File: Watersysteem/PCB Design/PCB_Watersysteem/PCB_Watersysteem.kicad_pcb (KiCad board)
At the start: 2 copper layers, 98 parts, among them J1 12V ingang, J10 LED Water Level, J11 LED Nutrient Level, J12 Height Nutrients, J13 Height Mixer, J14 Pomp1, J15 Pomp2, J16 Pomp3, J17 Pomp4, J18 Luchtpomp, J19 Mixer, J2 TTL Connector, J20 UV, J22 230V, J23 ReferentieProbe, J24 Voedingsstoffen 1, J25 Voedingsstoffen 2, J26 Voedingsstoffen 3, J6 Height Water, J7 Endstop Lade0, J8 Endstop Lade1, J9 Endstop UV, K1 AHQSS105DM2FA0G, K2 AHQSS105DM2FA0G, K3 AHQSS105DM2FA0G, K6 AHQSS105DM2FA0G, K7 AHQSS105DM2FA0G, K8 AHQSS105DM2FA0G, K9 AHQSS105DM2FA0G, Q1 BSS138, Q2 BSS138, Q3 BSS138, Q4 BSS138, Q5 BSS138, Q6 BSS138, Q7 BSS138, SW1 EN, SW2 BOOT, U1 ESP32-WROOM-32D, U2 MP1584_Module, U3 AMS1117-3.3, U4 ADS1115IDGS, U5 MCP23017_SO

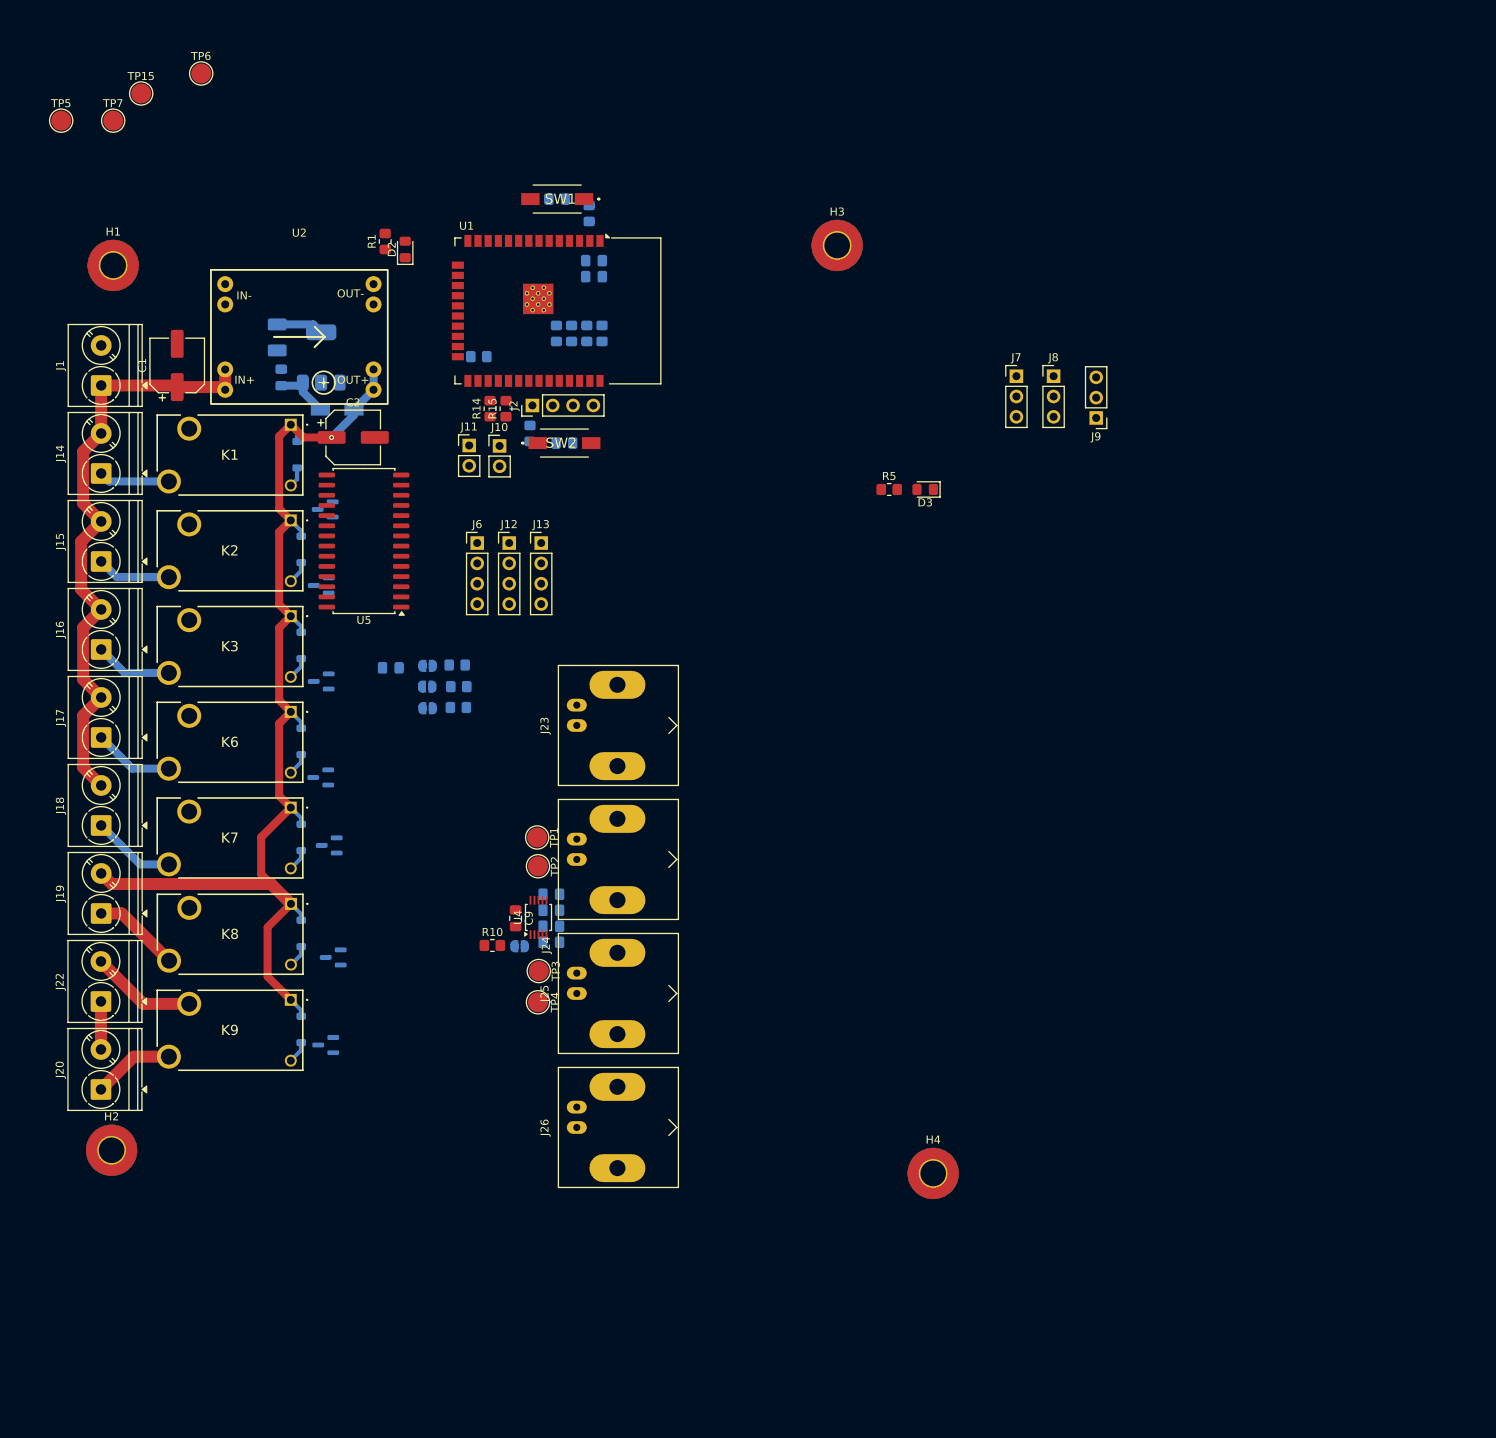
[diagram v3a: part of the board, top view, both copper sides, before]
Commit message: Update PCB
Placing en routing van vermogen, grootste componenten
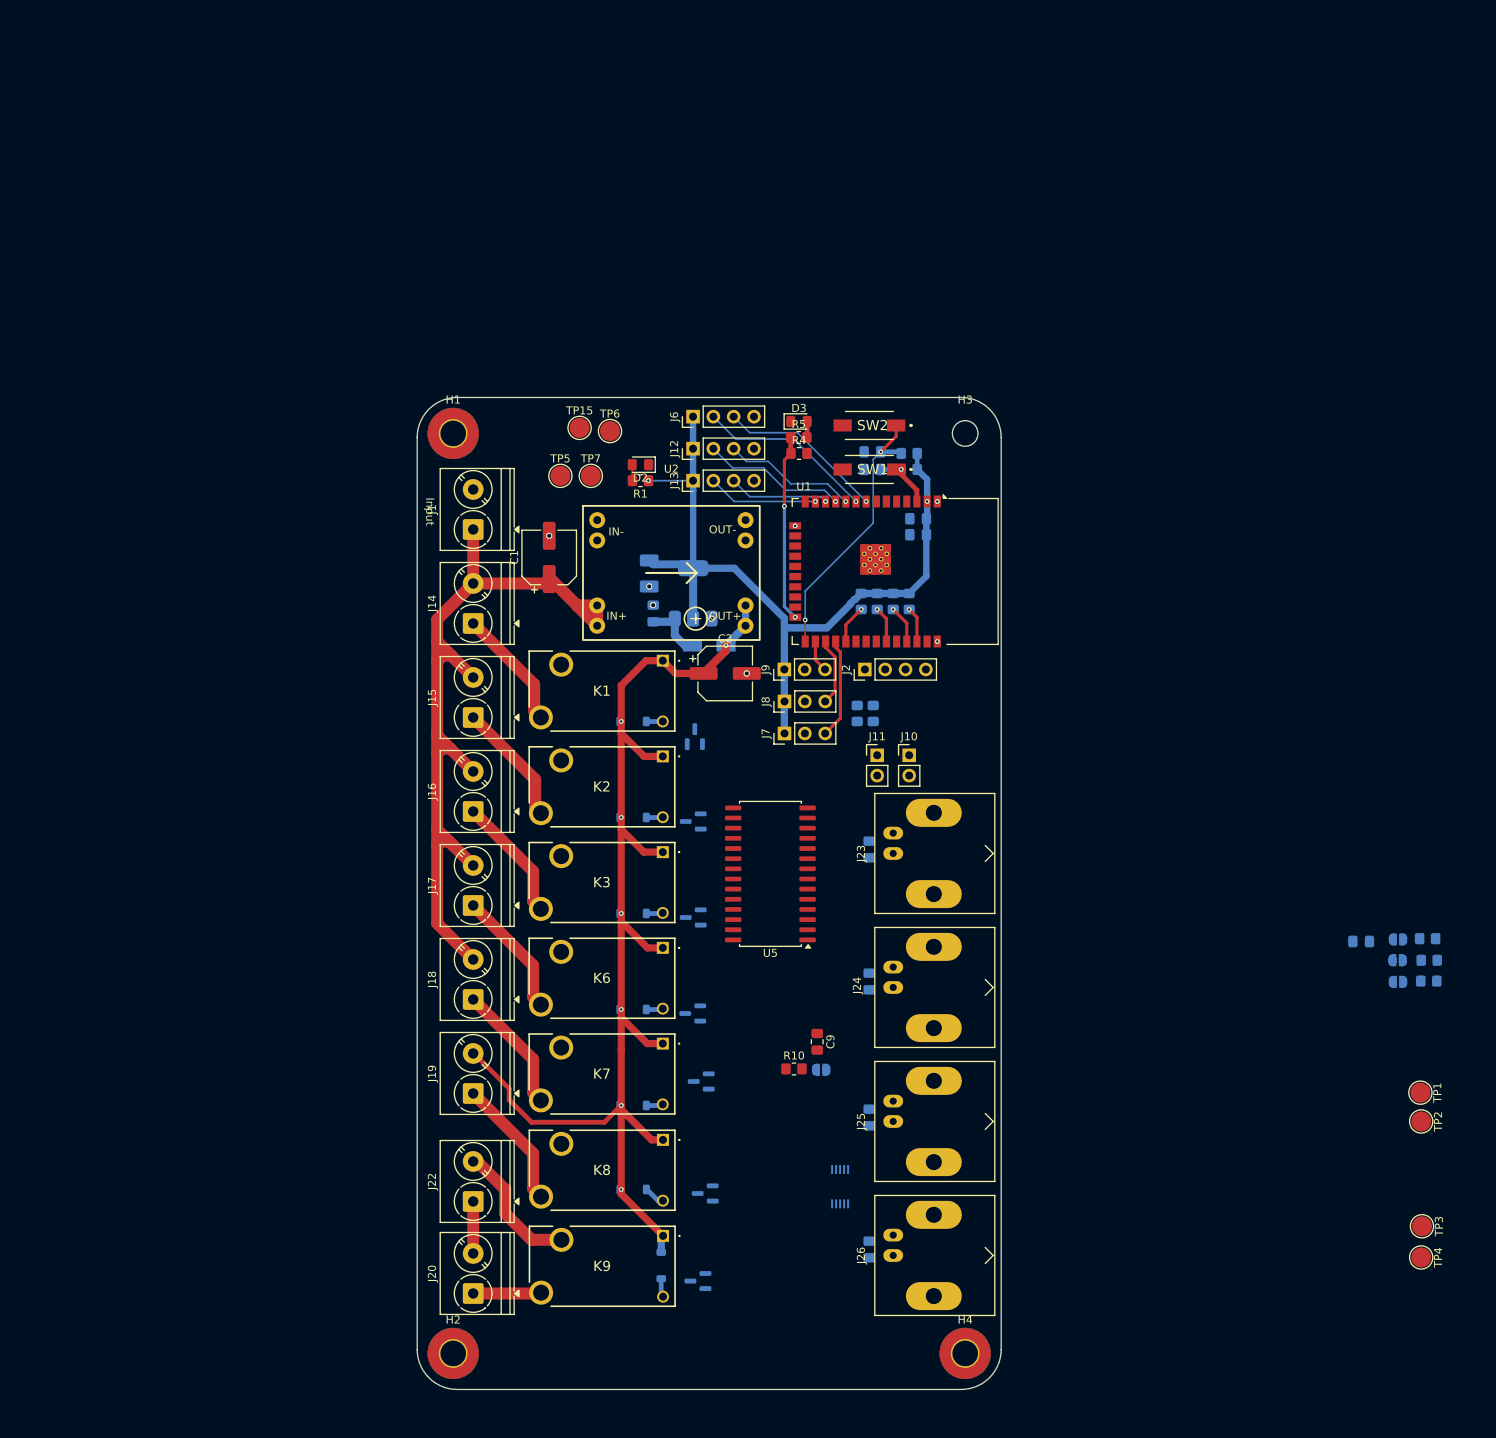
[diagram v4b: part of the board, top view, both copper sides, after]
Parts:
- H3: value MountingHole_Pad -> MountingHole; footprint MountingHole:MountingHole_3.2mm_M3_Pad_TopBottom -> MountingHole:MountingHole_3.2mm_M3
- R14, R15, U4: moved to B.Cu
- R4: moved to F.Cu
- moved JP3 126.0 mm to (163.1, 120.3)
- moved R13 126.0 mm to (166.8, 117.7)
- moved C14 126.0 mm to (158.5, 118.0)
- moved JP2 126.0 mm to (163.1, 117.8)
- moved JP4 126.0 mm to (163.1, 123.0)
- moved R11 126.0 mm to (167.0, 120.3)
- moved R12 126.0 mm to (166.9, 123.0)
- moved TP1 114.9 mm to (165.9, 136.9)
- moved TP2 114.9 mm to (166.0, 140.5)
- moved TP4 114.9 mm to (166.0, 157.5)
- moved TP3 114.9 mm to (166.1, 153.6)
- moved TP5 76.6 mm to (58.4, 59.8)
- moved TP7 74.4 mm to (62.2, 59.8)
- moved TP15 68.9 mm to (60.8, 53.8)
- moved TP6 67.9 mm to (64.6, 54.2)
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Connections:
- U1 pad 10: TRIG_NUT -> ECHO_NUT
- U1 pad 11: ECHO_NUT -> TRIG_NUT
- U1 pad 12: TRIG_MIX -> ECHO_MIX
- U1 pad 13: ECHO_MIX -> TRIG_MIX
- U1 pad 8: TRIG_WATER -> ECHO_WATER
- U1 pad 9: ECHO_WATER -> TRIG_WATER
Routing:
- net 3V3: track 5.90 -> 101.5 mm, vias 0 -> 2
- net GPIO0: track 0.00 -> 34.4 mm, vias 0 -> 2
- net 12V: track 75.9 -> 106.4 mm
- net GPIO2: track 0.00 -> 23.4 mm, vias 0 -> 2
- net TRIG_WATER: track 0.00 -> 22.2 mm, vias 0 -> 1
- net ECHO_WATER: track 0.00 -> 21.0 mm, vias 0 -> 1
- net TRIG_NUT: track 0.00 -> 18.0 mm, vias 0 -> 1
- net ECHO_NUT: track 0.00 -> 16.8 mm, vias 0 -> 1
- net TRIG_MIX: track 0.00 -> 13.8 mm, vias 0 -> 1
- net ECHO_MIX: track 0.00 -> 12.6 mm, vias 0 -> 1
- net ENDSTOP1: track 0.00 -> 12.5 mm
- net 5V: track 141.8 -> 152.5 mm, vias 1 -> 7
- net ENDSTOP2: track 0.00 -> 8.50 mm
- net ENABLE: track 0.00 -> 8.26 mm, vias 0 -> 1
- net PUMP1: track 8.87 -> 15.3 mm
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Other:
- board outline added: 73 x 124 mm
- board text added: "Input"

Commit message: Update PCB
Alle connecties gemaakt
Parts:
- removed TP5, TP6: TestPoint, TestPoint:TestPoint_Pad_D2.5mm
- JP1, JP2, JP3, JP4: moved to F.Cu
- moved R12 84.6 mm to (85.3, 100.6), turned to 180 degrees
- moved R11 84.5 mm to (85.3, 98.5)
- moved R13 82.8 mm to (85.3, 102.8)
- moved JP4 82.0 mm to (85.0, 98.2), turned to 180 degrees
- moved JP3 80.5 mm to (85.0, 100.7), turned to 180 degrees
- moved JP2 79.5 mm to (85.0, 103.2), turned to 180 degrees
- moved TP4 78.5 mm to (88.8, 143.4)
- moved C14 74.4 mm to (85.3, 104.9)
- moved TP3 71.8 mm to (95.2, 142.2)
- moved TP1 71.2 mm to (94.8, 134.0)
- moved TP2 70.6 mm to (95.4, 138.6)
- moved C10 27.7 mm to (93.4, 134.0), turned to 180 degrees
- moved C12 14.8 mm to (90.0, 143.5), turned to 0 degrees
- moved C13 14.5 mm to (95.8, 137.5)
- moved J2 14.5 mm to (86.4, 94.5)
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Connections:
- C10 pad 1: Nutr0 -> RefProbe
- J23 pad 1: Nutr0 -> RefProbe
- TP1 pad 1: Nutr0 -> RefProbe
- U4 pad 4: Nutr0 -> Nutr1
- U4 pad 5: Nutr1 -> Nutr2
- U4 pad 6: Nutr2 -> Nutr3
- U4 pad 7: Nutr3 -> RefProbe
- U5 pad 25: RELAY_UV -> RELAY_AIR
- U5 pad 26: RELAY_AIR -> RELAY_UV
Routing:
- net SDA0: track 4.48 -> 73.7 mm, vias 1 -> 2
- net 3V3: track 101.5 -> 169.8 mm, vias 2 -> 7
- net SCL0: track 4.40 -> 70.9 mm, vias 1 -> 2
- net RELAY_UV: track 0.00 -> 42.1 mm, vias 0 -> 1
- net RefProbe: track 0.00 -> 38.7 mm, vias 0 -> 1
- net RELAY_MIXER: track 0.00 -> 27.4 mm, vias 0 -> 1
- net RX0: track 0.00 -> 23.7 mm, vias 0 -> 1
- net TX0: track 4.70 -> 26.6 mm, vias 1 -> 2
- net Nutr3: track 0.00 -> 21.1 mm, vias 0 -> 1
- net RELAY_PUMP1: track 0.00 -> 21.1 mm, vias 0 -> 1
- net Nutr1: track 0.00 -> 20.3 mm, vias 0 -> 1
- net RELAY_AIR: track 0.00 -> 17.9 mm, vias 0 -> 1
- net RELAY_PUMP2: track 0.00 -> 11.6 mm, vias 0 -> 1
- net Net-(JP4-B): track 0.00 -> 10.1 mm, vias 0 -> 1
- net Net-(JP3-B): track 0.00 -> 8.94 mm, vias 0 -> 1
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
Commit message: Silkscreen
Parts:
- Nutriënt 1: renamed from J24
- Nutriënt 2: renamed from J25
- Nutriënt 3: renamed from J26
- moved TP1 21.3 mm to (95.2, 112.7)
- moved TP4 9.71 mm to (94.0, 151.6)
- moved TP2 9.50 mm to (95.3, 129.1)
- moved C14 2.70 mm to (82.6, 105.0)
- moved JP2 2.70 mm to (82.2, 103.3)
- moved JP3 2.70 mm to (82.2, 100.8)
- moved JP4 2.70 mm to (82.2, 98.3)
- moved R12 2.70 mm to (82.7, 100.8)
- moved R13 2.70 mm to (82.7, 102.9)
- moved R11 2.70 mm to (82.7, 98.6)
- moved Program 2.50 mm to (86.4, 97.0)
- moved TP3 1.97 mm to (93.5, 141.2)
- moved Mixer 0.80 mm to (75.0, 59.6)
- moved Nutr 0.60 mm to (75.0, 55.8)
- moved 3V3 0.50 mm to (62.7, 60.4)
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- renumbered J7 to 1, J8 to 2, J9 to 3, TP7 to 3V3, TP15 to GND, J13 to Mixer, J11 to Nutr, J12 to Nutr, J2 to Program, J23 to Referentie, J6 to Water, J10 to Water
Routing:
- net Nutr1: track 20.3 -> 22.9 mm
- net TX0: track 26.6 -> 29.1 mm
- net RX0: track 23.7 -> 26.2 mm
- net RefProbe: track 38.7 -> 41.1 mm
- net GND: track 1.58 -> 0.00 mm
- net Net-(JP3-B): track 8.94 -> 7.63 mm
- net Net-(JP2-B): track 7.75 -> 6.50 mm
- net ENDSTOP2: track 8.52 -> 7.52 mm
- net Net-(JP4-B): track 10.1 -> 9.13 mm
- net ENDSTOP1: track 12.1 -> 11.1 mm
- net TRIG_MIX: track 13.8 -> 14.6 mm
- net ECHO_MIX: track 12.6 -> 13.4 mm
- net Nutr2: track 8.36 -> 9.15 mm
- net 3V3: track 169.8 -> 170.4 mm
- net TRIG_NUT: track 18.0 -> 18.6 mm
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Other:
- board text added: "+"
- board text added: "-"
- board text added: "12V Input"
- board text added: "230V input"
- board text added: "3V|Gnd|In"
- board text added: "3V|Rx|Tx|Gnd"
- board text added: "3V|Tx|Rx|Gnd"
- board text added: "Eindeloop"
- board text added: "Hoogte"
- board text added: "LED"
- board text added: "Lucht"
- board text added: "Mixer"
- board text added: "Nutr"
- board text added: "Pomp 1"
- board text added: "Pomp 2"
- board text added: "Pomp 3"
- board text added: "Pomp 4"
- board text added: "Programming"
- board text added: "UV"
- board text added: "Water"
- board text removed: "Input"

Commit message: Afwerking
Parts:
- removed 3V3, GND: TestPoint, TestPoint:TestPoint_Pad_D2.5mm
- added G***: LOGO, LOGO, F.Cu at (54.5, 169.4)
- added G***: LOGO, LOGO, F.Cu at (83.9, 169.5)
- added G***: LOGO, LOGO, B.Cu at (54.5, 169.6)
- added J3: Backup GPIO, Connector_PinHeader_2.54mm:PinHeader_1x06_P2.54mm_Vertical, F.Cu at (91.9, 108.8)
- added J4: TestPins, Connector_PinHeader_2.54mm:PinHeader_1x02_P2.54mm_Vertical, F.Cu at (62.6, 60.3)
- J24: renamed from Nutriënt 1
- J25: renamed from Nutriënt 2
- J26: renamed from Nutriënt 3
- TP1, TP2, TP3, TP4: footprint TestPoint:TestPoint_Pad_D2.5mm -> TestPoint:TestPoint_Pad_D2.0mm
- moved TP1 0.85 mm to (95.8, 112.1)
- renumbered Water to J10, Nutr to J11, Nutr to J12, Mixer to J13, Program to J2, Referentie to J23, Water to J6, 1 to J7, 2 to J8, 3 to J9
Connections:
- U5 pad 5: unconnected-(U5-GPB4-Pad5) -> Net-(J3-Pin_6)
- U5 pad 6: unconnected-(U5-GPB5-Pad6) -> Net-(J3-Pin_5)
- U5 pad 7: unconnected-(U5-GPB6-Pad7) -> Net-(J3-Pin_4)
- U5 pad 8: unconnected-(U5-GPB7-Pad8) -> Net-(J3-Pin_3)
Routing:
- net GND: track 0.00 -> 12.5 mm, vias 17 -> 48
- net Net-(J3-Pin_6): track 0.00 -> 6.25 mm
- net Net-(J3-Pin_5): track 0.00 -> 5.08 mm
- net Net-(J3-Pin_4): track 0.00 -> 4.11 mm
- net Net-(J3-Pin_3): track 0.00 -> 3.58 mm
- net SDA0: track 73.7 -> 70.2 mm, vias 2 -> 3
- net RX0: track 26.2 -> 24.5 mm, vias 1 -> 0
- net TX0: track 29.1 -> 27.7 mm, vias 2 -> 1
- net SCL0: track 70.9 -> 69.7 mm
- net 3V3: track 170.4 -> 170.9 mm, vias 7 -> 6
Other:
- board text added: "1"
- board text added: "2"
- board text added: "3"
- board text added: "B7|B6|B5|B4|Gnd|Gnd"
- board text added: "BOOT"
- board text added: "Backup IO"
- board text added: "Charlotte Bert Sander Haustraete Kjell Naessens Niels Verhoeve"
- board text added: "ENABLE"
- board text added: "Gnd 3V3"
- board text added: "Mix"
- board text added: "Nutriënten 1"
- board text added: "Nutriënten 2"
- board text added: "Nutriënten 3"
- board text added: "Referentie"
- board text added: "Watersysteem"
